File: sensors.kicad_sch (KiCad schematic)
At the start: 14 parts, among them J4 Hirose U.FL, U3 ICM-42688-P, U4 NEO-M8M

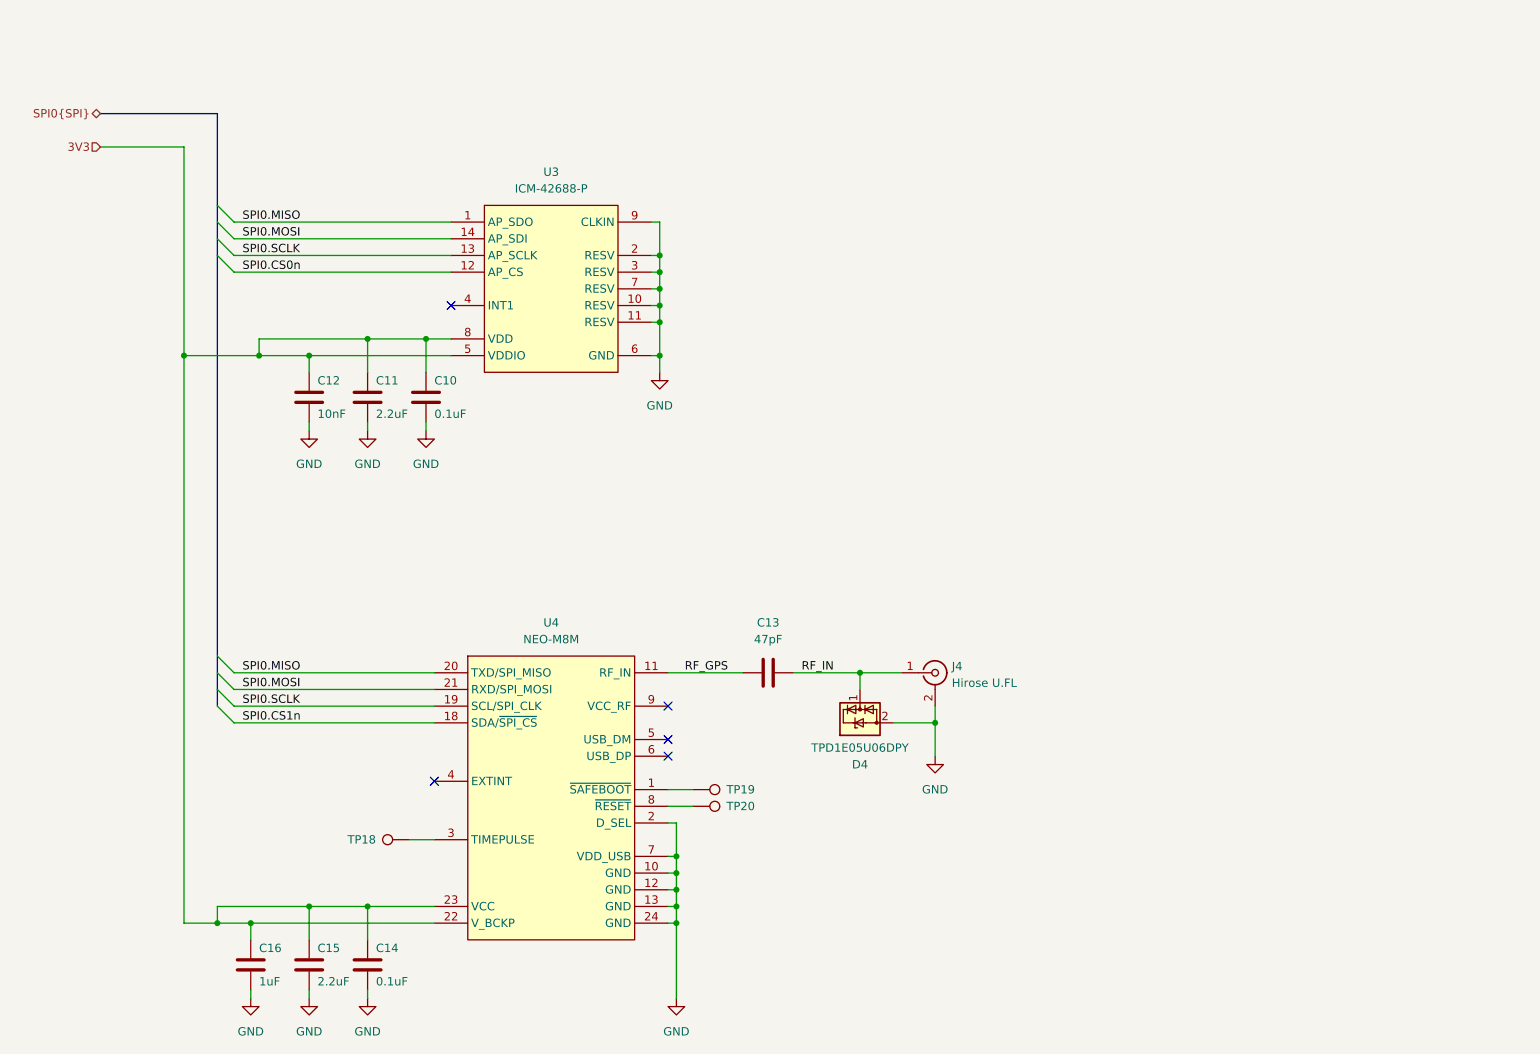
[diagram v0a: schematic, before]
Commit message: added temp sensors
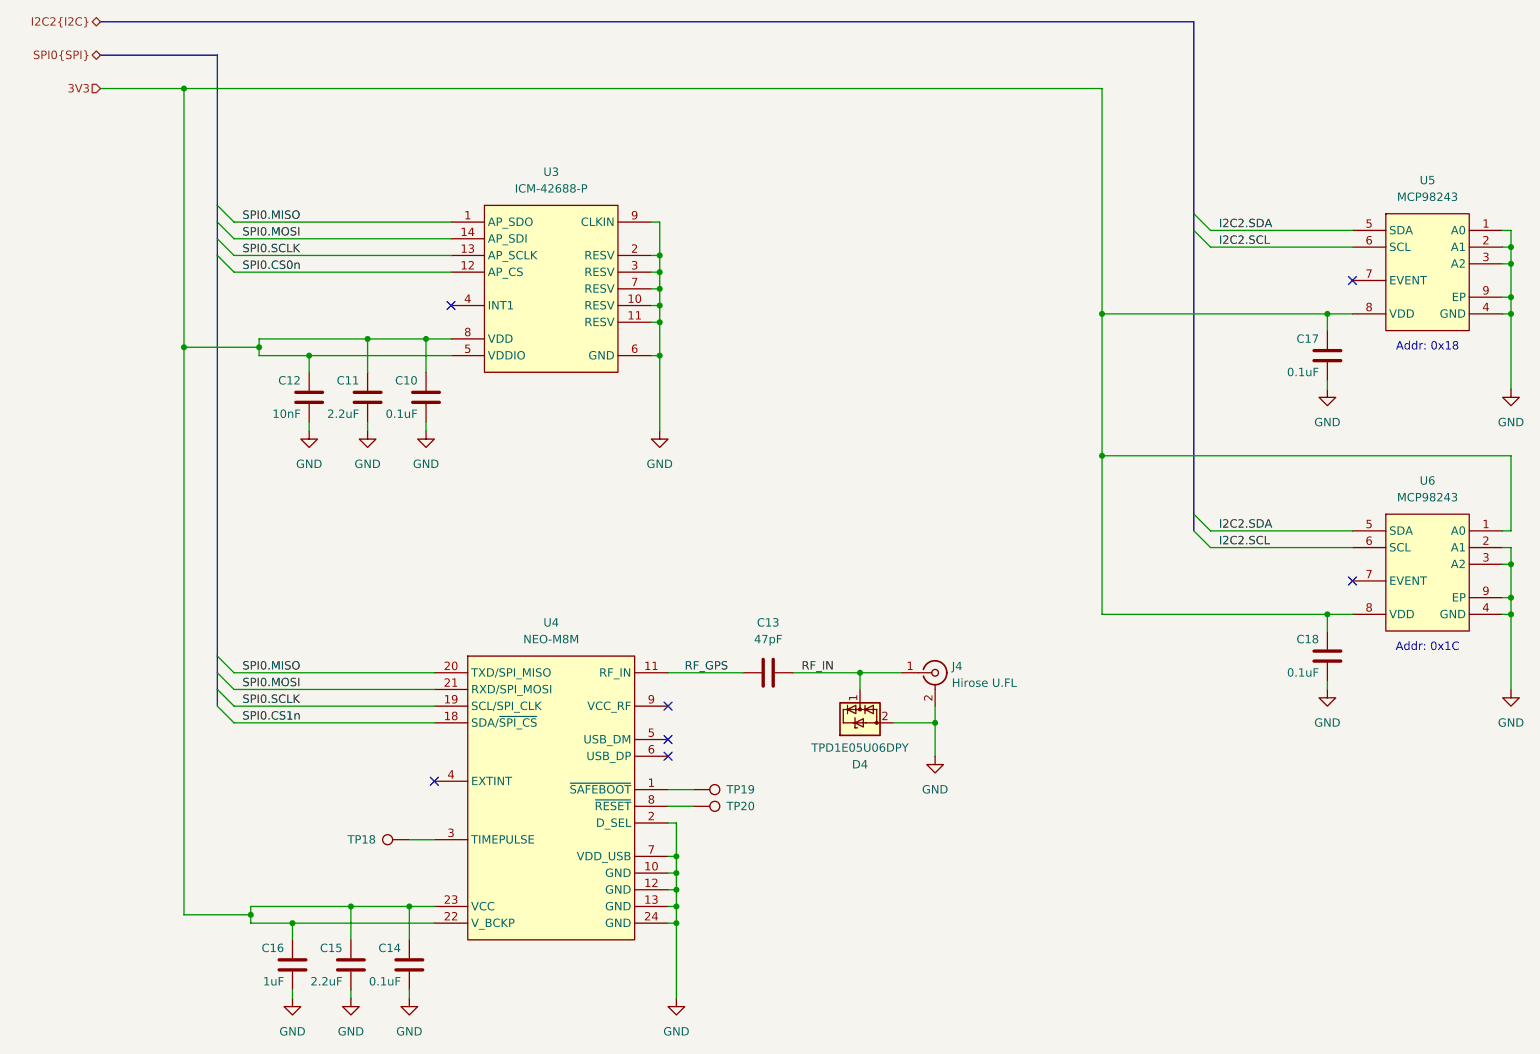
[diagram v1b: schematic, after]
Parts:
- added C17, C18: 0.1uF, Capacitor_SMD:C_0402_1005Metric, symbol library:C
- added U5, U6: MCP98243, Package_DFN_QFN:DFN-8-1EP_3x2mm_P0.5mm_EP1.3x1.5mm, symbol library:MCP98243
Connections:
- net 3V3: now also C17.1, C18.1, U5.8 (VDD), U6.1 (A0), U6.8 (VDD)
- net GND: now also C17.2, C18.2, U5.1 (A0), U5.2 (A1), U5.3 (A2), U5.4 (GND), U5.9 (EP), U6.2 (A1), U6.3 (A2), U6.4 (GND), U6.9 (EP)
- new net I2C2.SCL: U5.6 (SCL), U6.6 (SCL)
- new net I2C2.SDA: U5.5 (SDA), U6.5 (SDA)
- no-connect marks 5 -> 7
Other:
- note added: "Addr: 0x18"
- note added: "Addr: 0x1C"
- moved on the sheet: C14, C15, C16

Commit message: corrected temp sens i2c addr
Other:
- note added: "Addr: 0x19"
- note removed: "Addr: 0x1C"
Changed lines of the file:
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@@
 		(company "Andre S Winkel | Highlander Space Program | University of California, Riverside")
 	)
-	(text "Addr: 0x1C"
+	(text "Addr: 0x19"
 		(exclude_from_sim no)
 		(at 238.76 114.3 0)

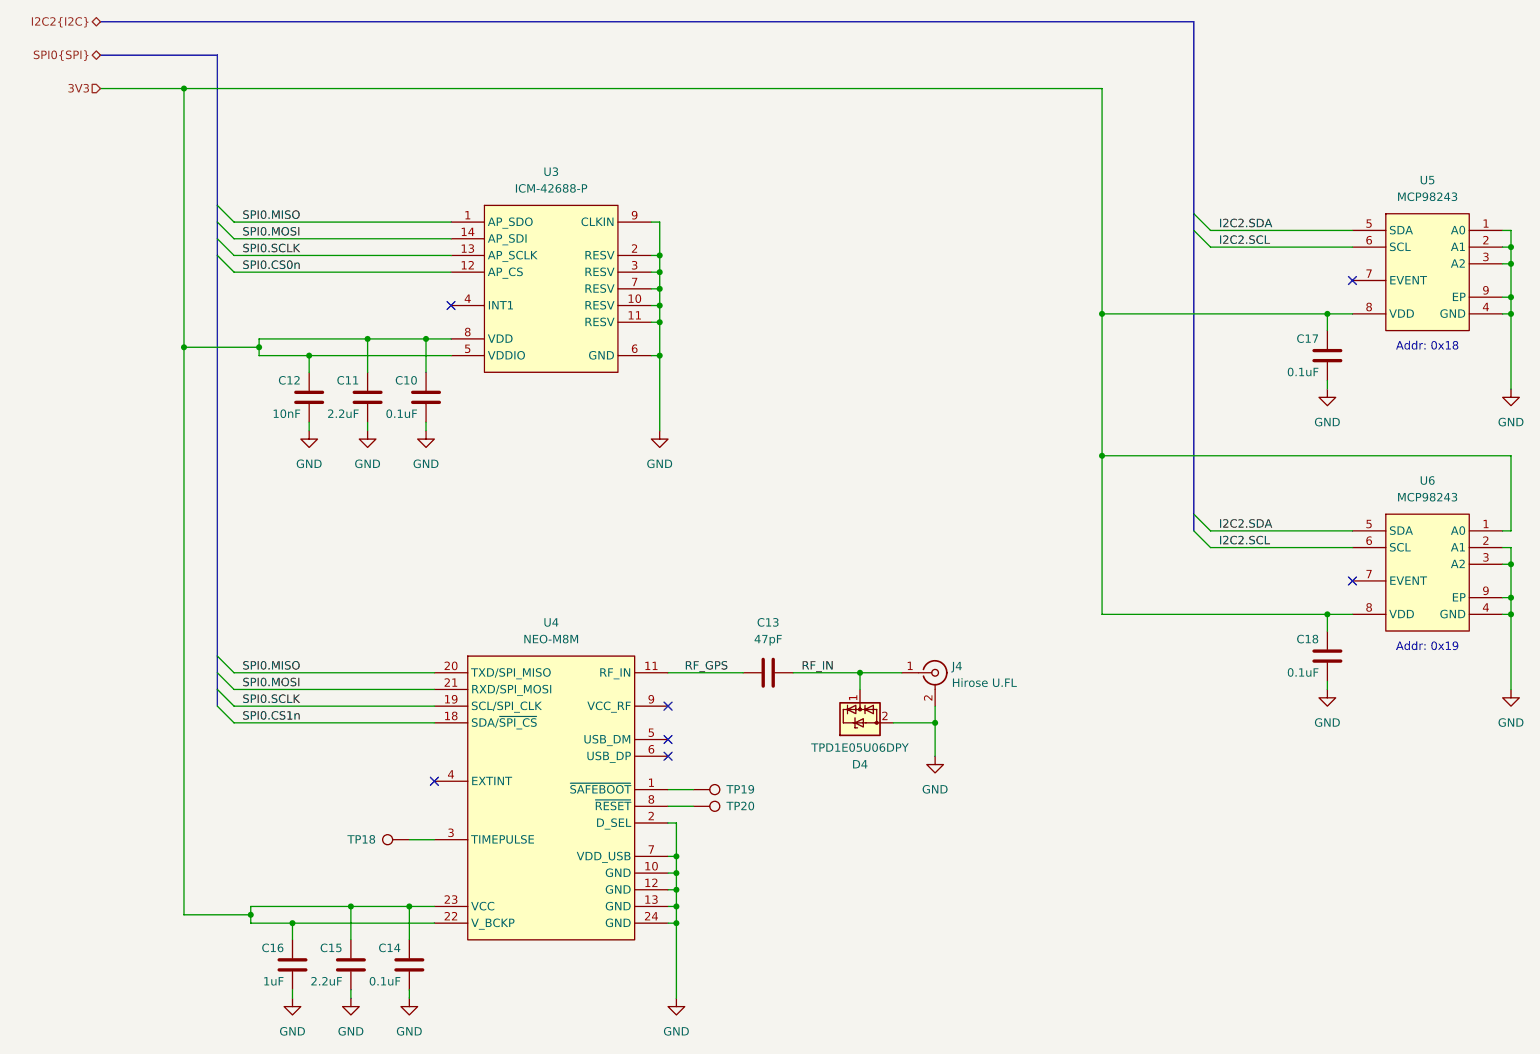
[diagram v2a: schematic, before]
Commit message: removed ublox
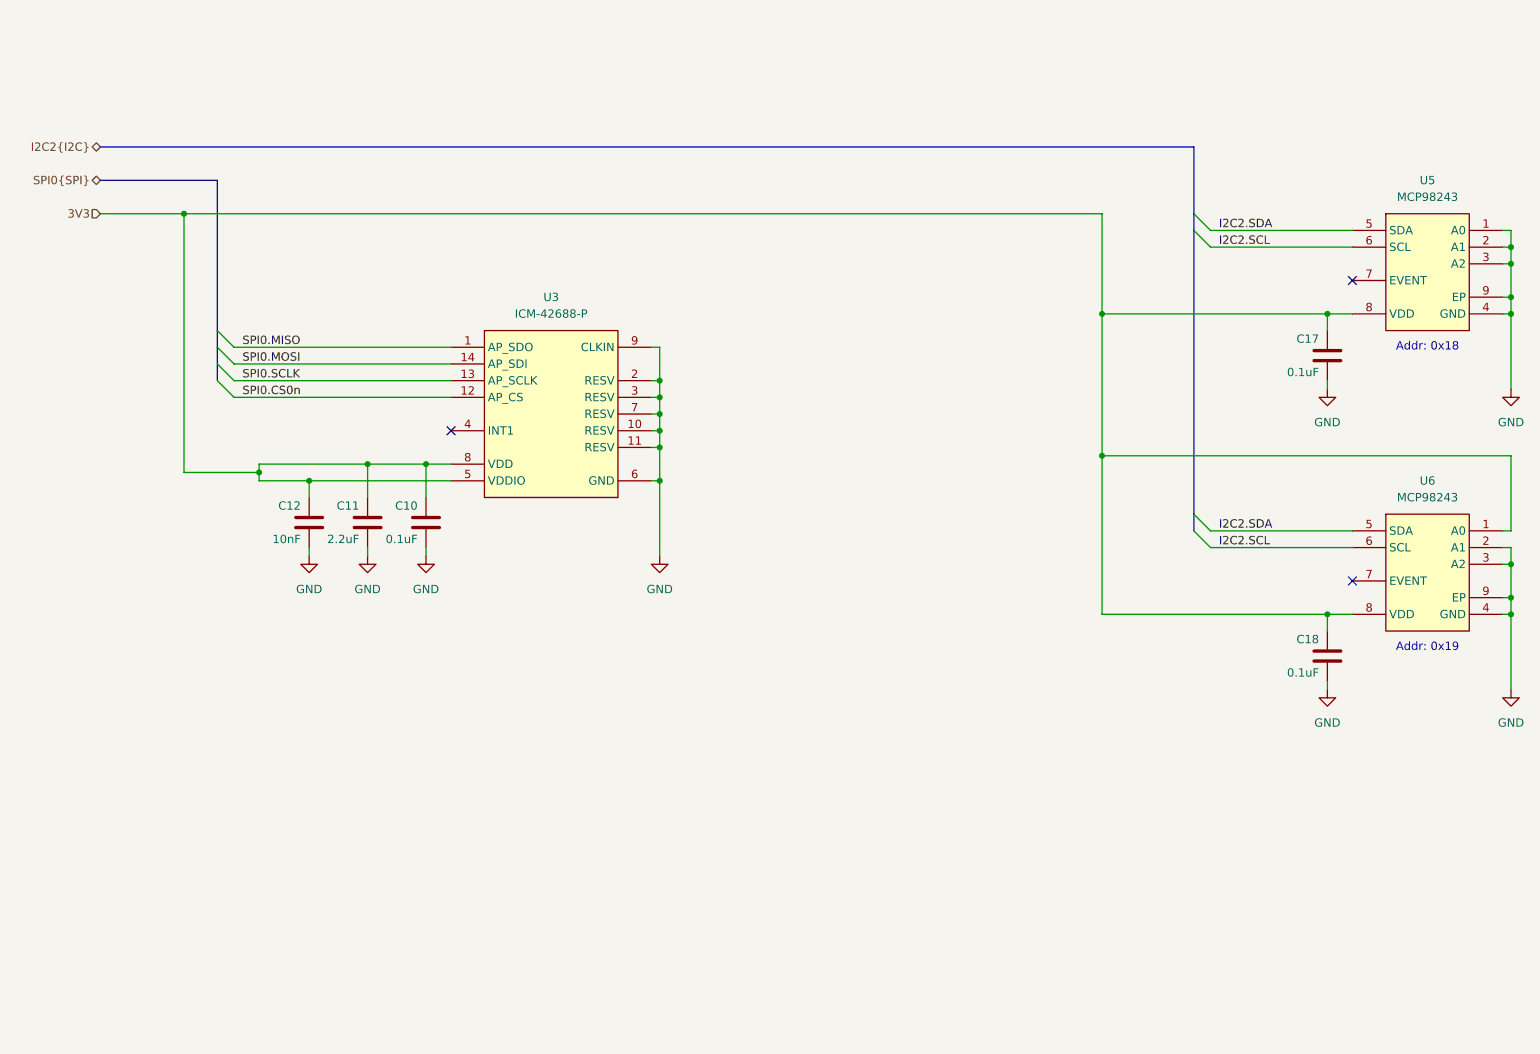
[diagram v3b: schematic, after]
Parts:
- removed C13: 47pF, Capacitor_SMD:C_0402_1005Metric, symbol library:C
- removed C14: 0.1uF, Capacitor_SMD:C_0402_1005Metric, symbol library:C
- removed C15: 2.2uF, Capacitor_SMD:C_0402_1005Metric, symbol library:C
- removed C16: 1uF, Capacitor_SMD:C_0402_1005Metric, symbol library:C
- removed D4: TPD1E05U06DPY, Package_SON:Texas_DPY0002A_0.6x1mm_P0.65mm, symbol library:TPD1E05U06DPY
- removed J4: Hirose U.FL, Connector_Coaxial:U.FL_Hirose_U.FL-R-SMT-1_Vertical, symbol library:Conn_Coaxial
- removed TP18, TP19, TP20: TestPoint, TestPoint:TestPoint_Pad_D1.0mm, symbol library:TestPoint
- removed U4: NEO-M8M, RF_GPS:ublox_NEO, symbol library:NEO-M8M
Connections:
- no-connect marks 7 -> 3
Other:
- moved on the sheet: C10, C11, C12, U3

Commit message: finished defining spi/i2c gpio, CAN, off-board signals
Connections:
- net SPI0.CS0n renamed SPI1.CS0n
- net SPI0.MISO renamed SPI1.MISO
- net SPI0.MOSI renamed SPI1.MOSI
- net SPI0.SCLK renamed SPI1.SCLK
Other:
- moved on the sheet: C10, C11, C12, C17, C18, U3, U5, U6

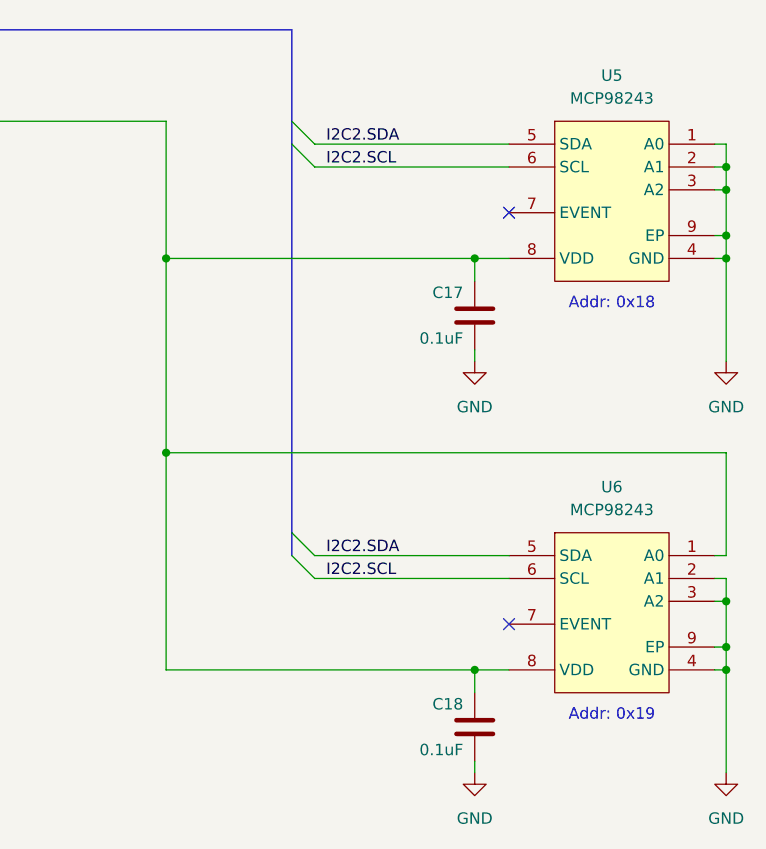
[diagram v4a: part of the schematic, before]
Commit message: redid gpio layout, removed one temp sensor, bom
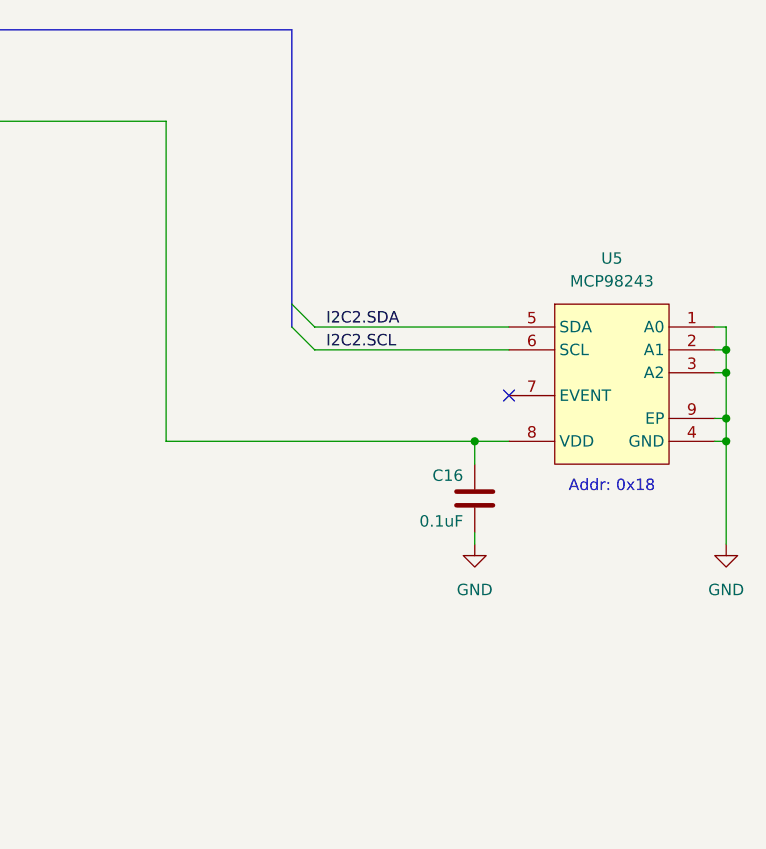
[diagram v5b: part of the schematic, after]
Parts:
- removed C17, C18: 0.1uF, Capacitor_SMD:C_0402_1005Metric, symbol library:C
- removed U6: MCP98243, Package_DFN_QFN:DFN-8-1EP_3x2mm_P0.5mm_EP1.3x1.5mm, symbol library:MCP98243
- added C16: 0.1uF, Capacitor_SMD:C_0402_1005Metric, symbol library:C
- C10: Field4 Farnell -> (none); Field5 2611911 -> (none); Field6 RM EMK105 B7104KV-F -> (none); Field7 TAIYO YUDEN EUROPE GMBH -> (none); Field8 110091611 -> (none); Manufacturer (none) -> KEMET; Manufacturer Product Number (none) -> C0402C104K4RACTU; Part Description 0.1uF 10% 16V Ceramic Capacitor X7R 0402 (1005 Metric) -> (none)
- C11: Manufacturer (none) -> YAGEO; Manufacturer Product Number (none) -> CC0402KRX5R7BB225
- C12: Manufacturer (none) -> KEMET; Manufacturer Product Number (none) -> C0402C103K3REC7411
- U3: Manufacturer (none) -> TDK InvenSense; Manufacturer Product Number (none) -> ICM-42688-P
- U5: Manufacturer (none) -> Microchip Technology; Manufacturer Product Number (none) -> MCP98243T-BE/MNY
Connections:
- net 3V3: now also C16.1
- net GND: now also C16.2
- no-connect marks 3 -> 2
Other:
- note removed: "Addr: 0x19"
- moved on the sheet: U5
